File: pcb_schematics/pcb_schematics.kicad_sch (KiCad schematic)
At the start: 30 parts, among them J1 CUE_SJ1-352XNG, J2 Conn_01x01_Pin, SW1 SW_Push, SW2 Bourns PEC11R, SW7 Bourns PEC11R, SW8 Bourns PEC11R, U1 RPi_Pico_TH, U2 RDA5807M_Module, U3 LM386, U4 LM386

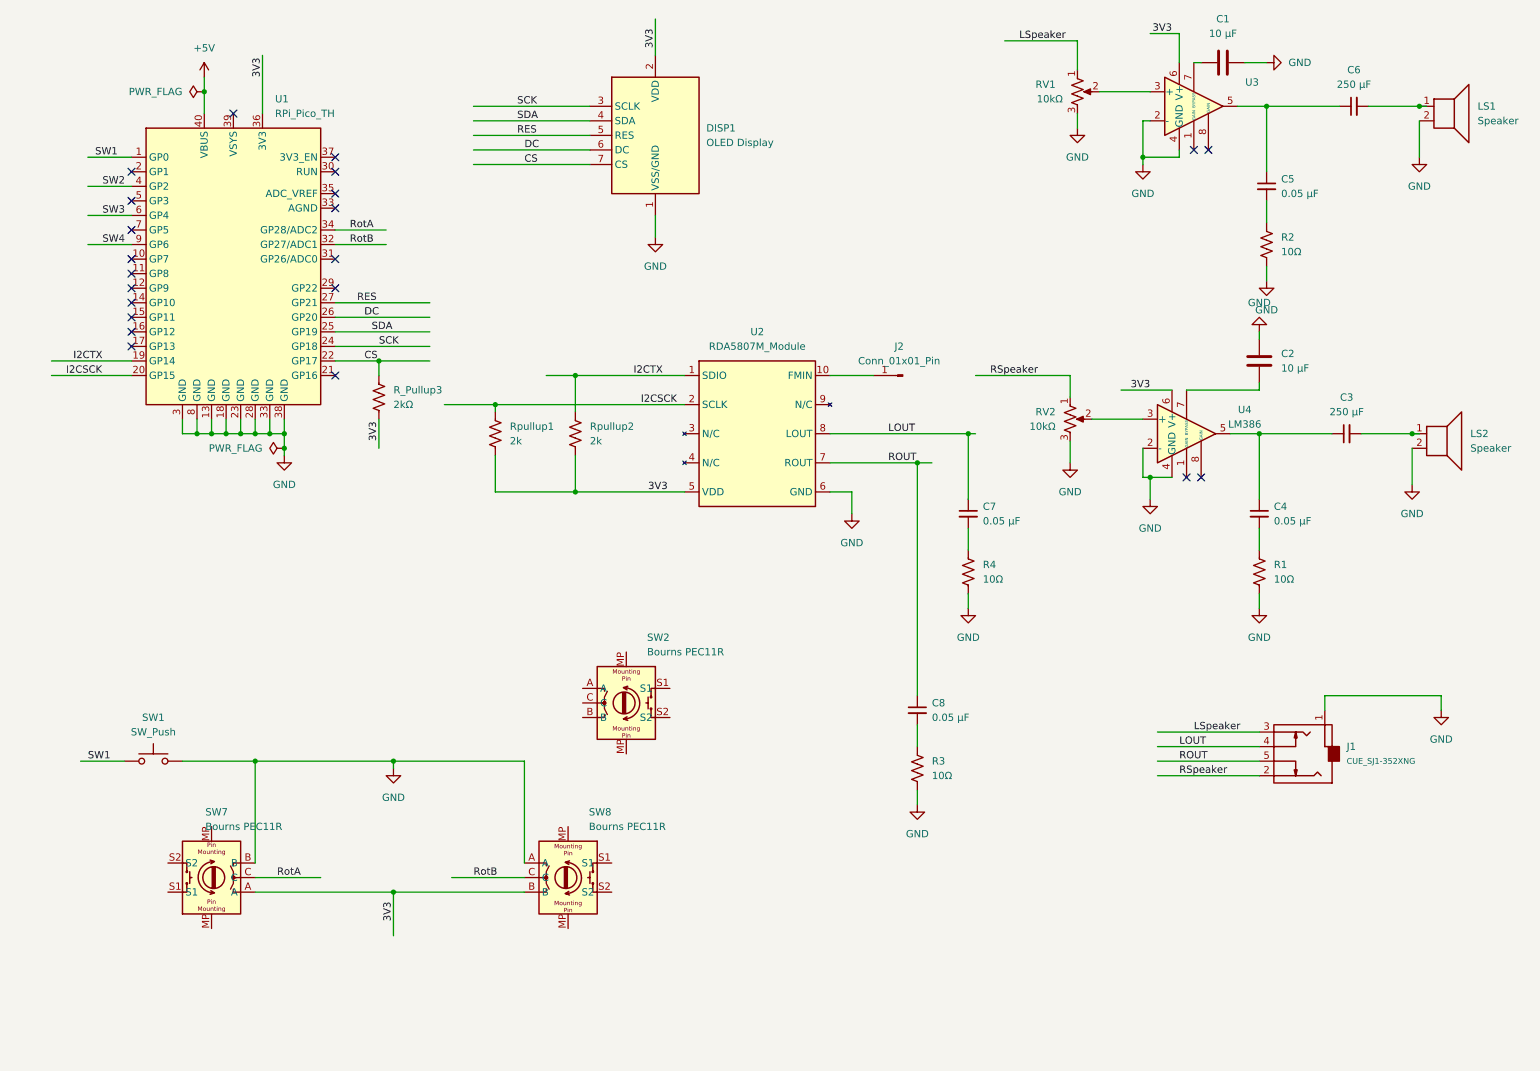
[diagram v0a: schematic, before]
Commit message: Converted to connectors
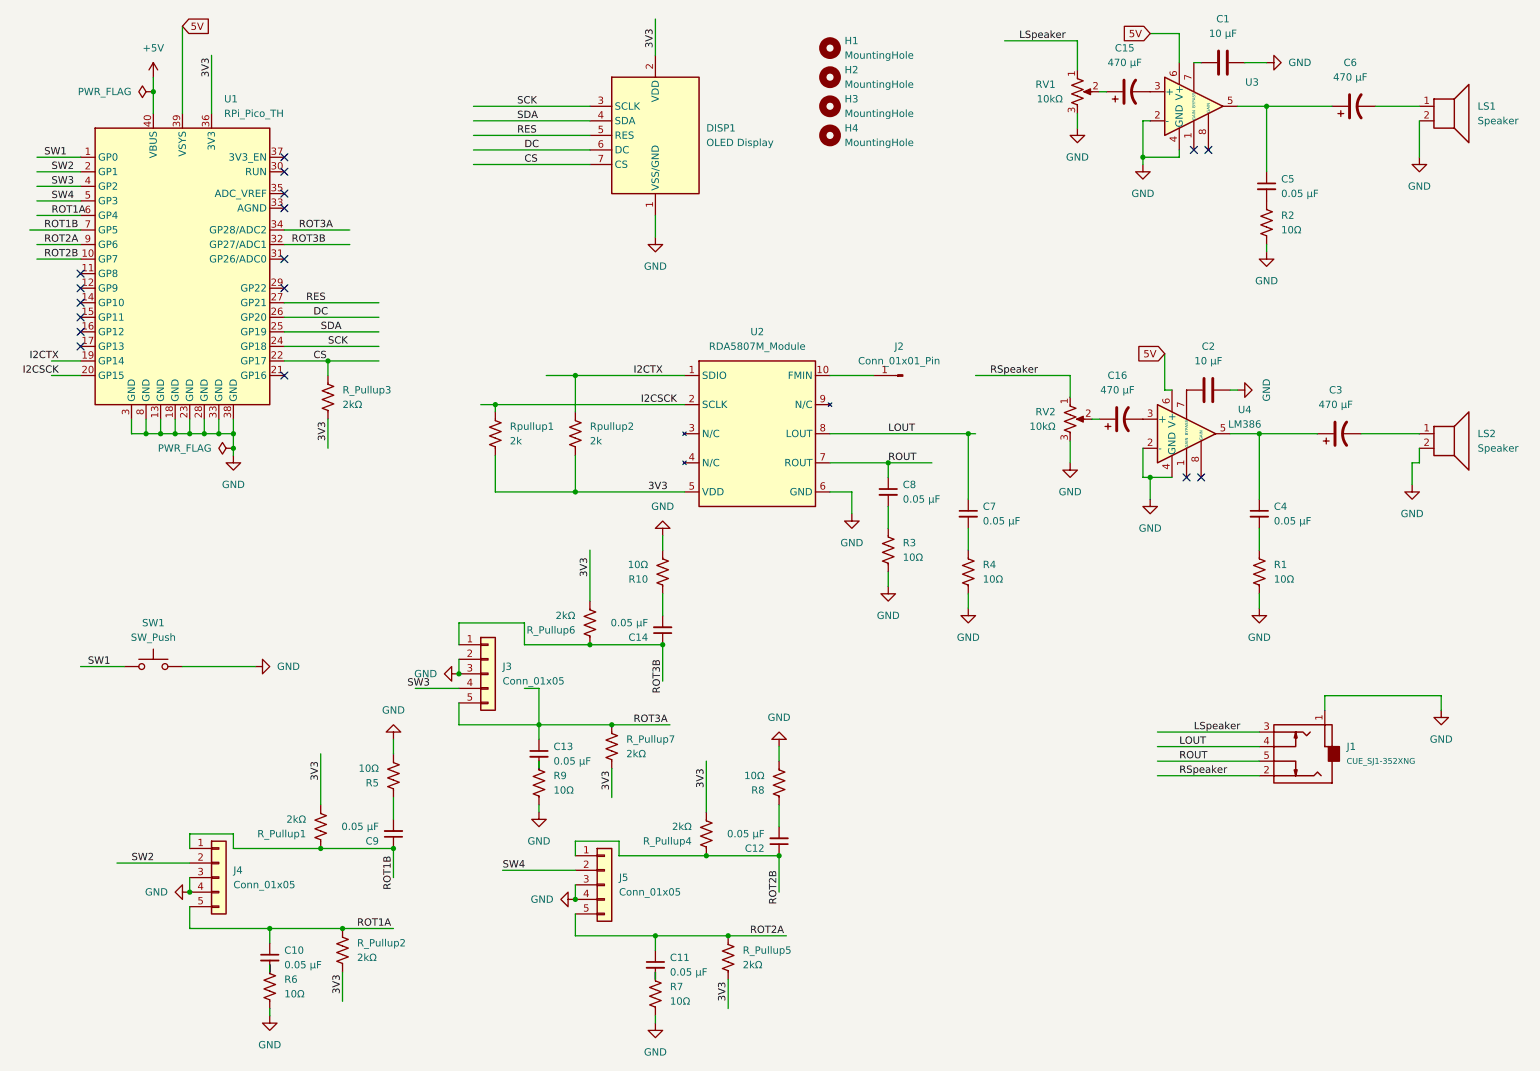
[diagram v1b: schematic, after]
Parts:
- removed C3, C6: 250 µF, symbol Device:C_Small
- removed SW2, SW7, SW8: Bourns PEC11R, Rotary_Encoder:RotaryEncoder_Alps_EC12E-Switch_Vertical_H20mm, symbol ECE:Bourns PEC11R
- added C10, C11, C12, C13, C14, C9: 0.05 µF, Capacitor_THT:C_Axial_L3.8mm_D2.6mm_P7.50mm_Horizontal, symbol Device:C_Small
- added C15, C16, C3, C6: 470 µF, Capacitor_THT:CP_Radial_D5.0mm_P2.50mm, symbol Device:C_Polarized_US
- added H1, H2, H3, H4: MountingHole, MountingHole:MountingHole_3.2mm_M3, symbol Mechanical:MountingHole
- added J3, J4, J5: Conn_01x05, Connector_PinHeader_2.00mm:PinHeader_1x05_P2.00mm_Vertical, symbol Connector_Generic:Conn_01x05
- added R10, R5, R6, R7, R8, R9: 10Ω, Resistor_THT:R_Axial_DIN0207_L6.3mm_D2.5mm_P10.16mm_Horizontal, symbol Device:R_US
- added R_Pullup1, R_Pullup2, R_Pullup4, R_Pullup5, R_Pullup6, R_Pullup7: 2kΩ, Resistor_THT:R_Axial_DIN0207_L6.3mm_D2.5mm_P10.16mm_Horizontal, symbol Device:R_US
- C4, C5, C7, C8: footprint (none) -> Capacitor_THT:C_Axial_L3.8mm_D2.6mm_P7.50mm_Horizontal
- J2: footprint Connector:Banana_Jack_1Pin -> Connector_Pin:Pin_D1.0mm_L10.0mm_LooseFit
- RV1, RV2: footprint ECE:Bourns_PTV09_Horiz -> Connector_PinHeader_2.54mm:PinHeader_1x03_P2.54mm_Vertical
- SW1: footprint Button_Switch_THT:Push_E-Switch_KS01Q01 -> Connector_PinHeader_1.27mm:PinHeader_1x02_P1.27mm_Vertical
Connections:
- net 3V3: now also R_Pullup1.2, R_Pullup2.2, R_Pullup4.2, R_Pullup5.2, R_Pullup6.2, R_Pullup7.2; no longer U3.6 (V+), U4.6 (V+)
- net GND: now also C2.2, J3.2 (Pin_2), J3.3 (Pin_3), J4.3 (Pin_3), J4.4 (Pin_4), J5.3 (Pin_3), J5.4 (Pin_4), R10.2, R5.2, R6.2, R7.2, R8.2, R9.2; no longer C2.1
- net SW2: now also U1.2 (GP1), J4.2 (Pin_2); no longer U1.4 (GP2)
- net SW3: now also U1.4 (GP2), J3.4 (Pin_4); no longer U1.6 (GP4)
- net SW4: now also U1.5 (GP3), J5.2 (Pin_2); no longer U1.9 (GP6)
- net at RV1.2: now also C15.1; no longer U3.3 (+)
- net at LS2.1: now also C3.2
- net at C5.1, U3.5: now also C6.1
- net at LS1.1: now also C6.2
- net ROT2B: now reaches U1.10 (GP7)
- net ROT2B: now also C12.1, J5.1 (Pin_1), R_Pullup4.1
- net 5V: now reaches U1.39 (VSYS)
- net 5V: now also U3.6 (V+), U4.6 (V+)
- net ROT1B: now reaches U1.7 (GP5)
- net ROT1B: now also C9.1, J4.1 (Pin_1), R_Pullup1.1
- net at C4.1, U4.5: now also C3.1
- net at RV2.2: now also C16.1; no longer U4.3 (+)
- net at U4.7 (BYPASS): now also C2.1; no longer C2.2
- net RotA renamed ROT3A
- net ROT3A: now also C13.1, J3.5 (Pin_5), R_Pullup7.1
- net RotB renamed ROT3B
- net ROT3B: now also C14.1, J3.1 (Pin_1), R_Pullup6.1
- new net: C12.2, R8.1
- new net: C15.2, U3.3 (+)
- new net: C16.2, U4.3 (+)
- new net: C10.2, R6.1
- new net: C9.2, R5.1
- new net: C13.2, R9.1
- new net: C14.2, R10.1
- new net: C11.2, R7.1
- new net ROT1A: C10.1, J4.5 (Pin_5), R_Pullup2.1, U1.6 (GP4)
- new net ROT2A: C11.1, J5.5 (Pin_5), R_Pullup5.1, U1.9 (GP6)
- no-connect marks 22 -> 17
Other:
- moved on the sheet: C2, C8, LS2, R2, R3, R_Pullup3, SW1, U1

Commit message: Updates PCb according to ROB's feedback
Added PCb layour according to the discussion with butoons and display on top and display below using front copper. Added Radio module using back copper. Speakers left to set up using back copper.
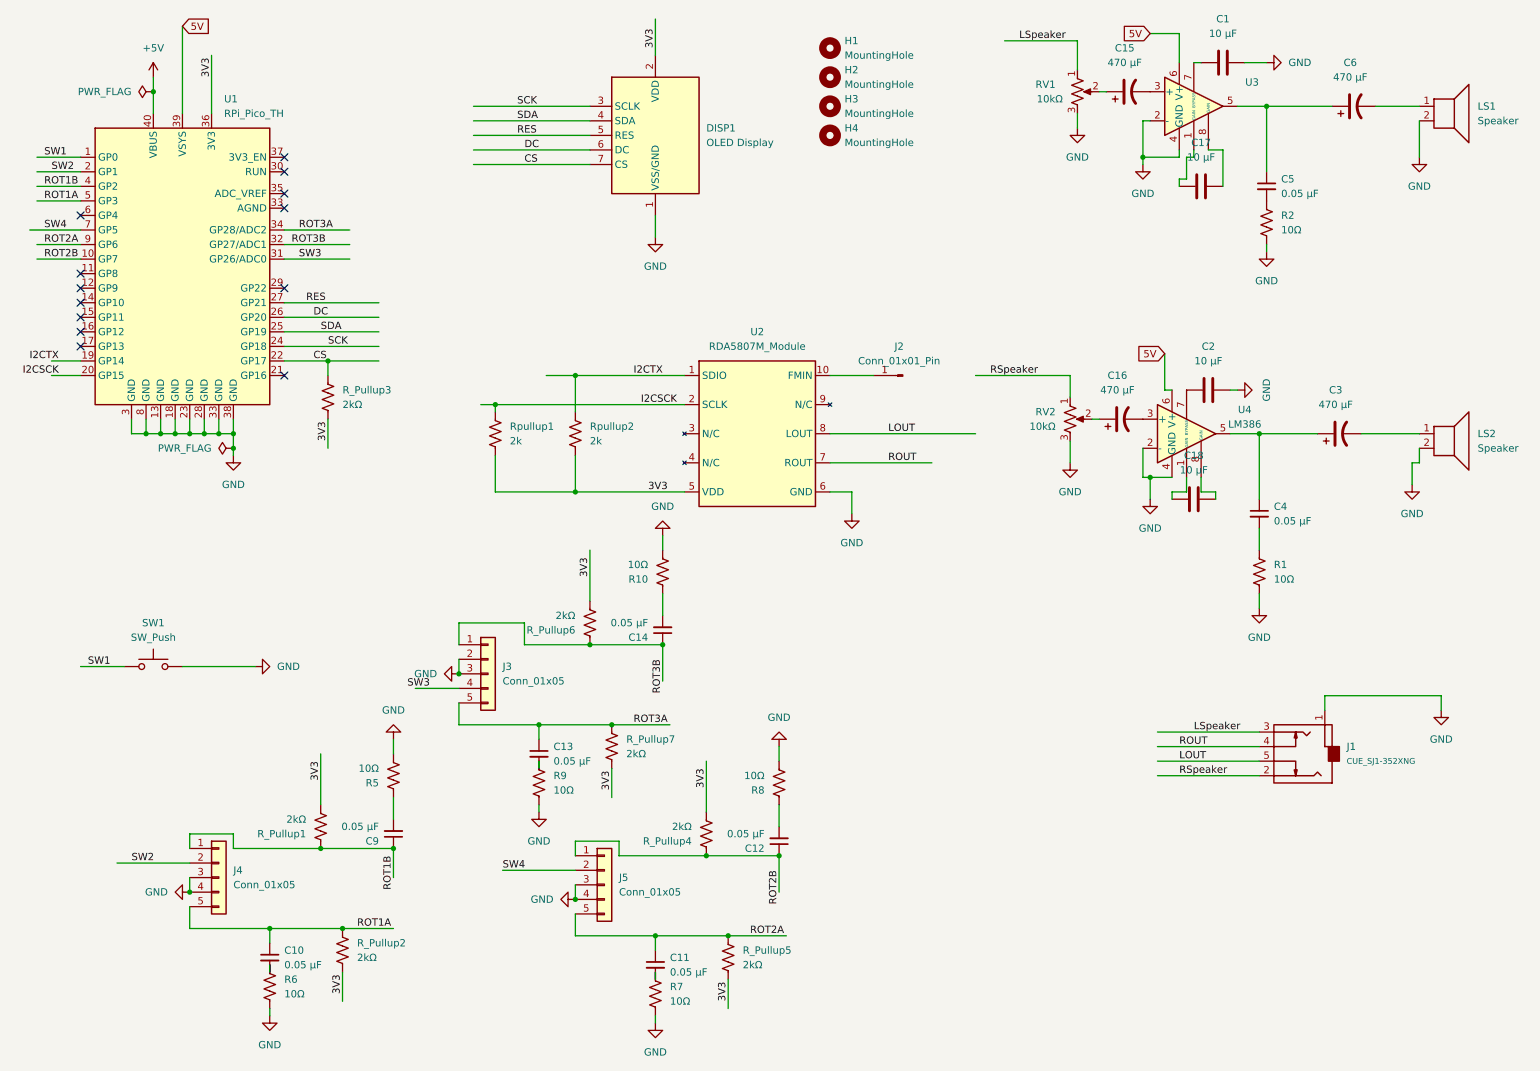
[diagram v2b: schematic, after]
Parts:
- removed C7, C8: 0.05 µF, Capacitor_THT:C_Axial_L3.8mm_D2.6mm_P7.50mm_Horizontal, symbol Device:C_Small
- removed R3, R4: 10Ω, Resistor_THT:R_Axial_DIN0207_L6.3mm_D2.5mm_P10.16mm_Horizontal, symbol Device:R_US
- added C17, C18: 10 µF, Capacitor_THT:CP_Radial_D6.3mm_P2.50mm, symbol Device:C
- C1, C2: footprint Capacitor_THT:CP_Radial_D5.0mm_P2.00mm -> Capacitor_THT:CP_Radial_D6.3mm_P2.50mm
- C15, C16, C3, C6: footprint Capacitor_THT:CP_Radial_D5.0mm_P2.50mm -> Capacitor_THT:CP_Radial_D6.3mm_P2.50mm
- LS1, LS2: footprint ECE:CUE_CMA-4544PF-W -> TerminalBlock_Phoenix:TerminalBlock_Phoenix_MKDS-1,5-2_1x02_P5.00mm_Horizontal
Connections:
- net LOUT: now also J1.5 (Ring_Switch); no longer J1.4 (Tip_Switch)
- net ROT1A: now also U1.5 (GP3); no longer U1.6 (GP4)
- net ROT1B: now also U1.4 (GP2); no longer U1.7 (GP5)
- net ROUT: now also J1.4 (Tip_Switch); no longer J1.5 (Ring_Switch)
- net SW3: now also U1.31 (GP26/ADC0); no longer U1.4 (GP2)
- net SW4: now also U1.7 (GP5); no longer U1.5 (GP3)
- net at U3.1 (GAIN): now also C17.1
- net at U3.8 (GAIN): now also C17.2
- net at U4.1 (GAIN): now also C18.1
- net at U4.8 (GAIN): now also C18.2
- no-connect marks 17 -> 13
